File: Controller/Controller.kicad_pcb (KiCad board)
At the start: 2 copper layers, 213 x 25 mm, 94 parts, among them J1 CON_TLC, J2 CON_15V, J3 CON_ICSP, J4 DC out, J5 CON_5V, J6 CON_5V_AUX, J7 CON_USB_A, Q1 SI4435FDY, Q2 SI4435FDY, Q3 SQ2309ES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

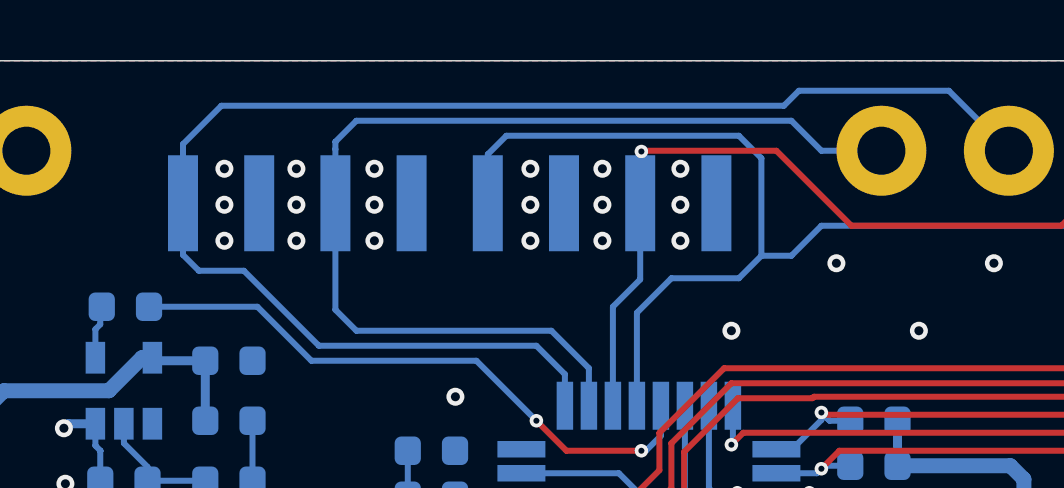
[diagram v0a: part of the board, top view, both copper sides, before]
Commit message: minor layout change.
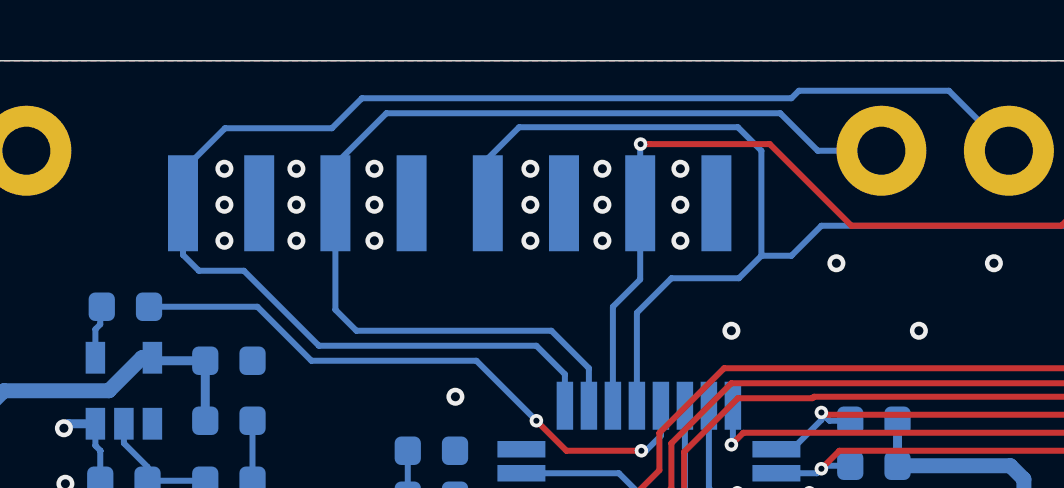
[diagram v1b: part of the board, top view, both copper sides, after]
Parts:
- removed the G*** at (239.0, 104.0)
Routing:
- net /TLC_BLANK: track 48.2 -> 47.7 mm

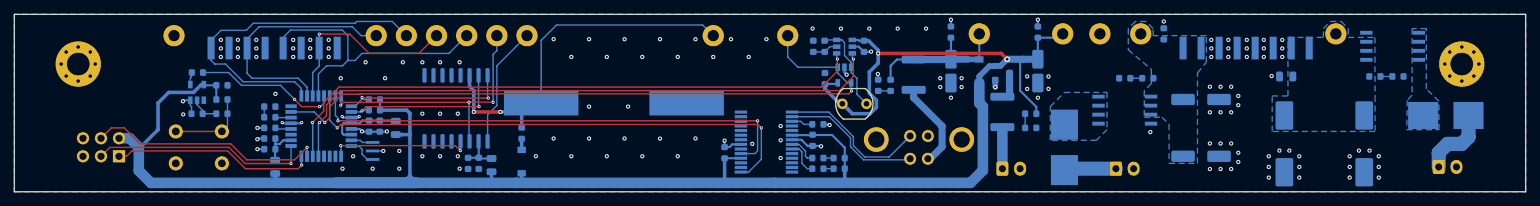
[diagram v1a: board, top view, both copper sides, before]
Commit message: Bug fixes: * Reset circuit   - netlabel RESET -> /RESET   - Reset button pulls high   - FTDI DTR connected to reset line * Added pull-ups to RTC outputs * Moved status LED to PC1 TODO: * Add thermal reliefs to copper planes
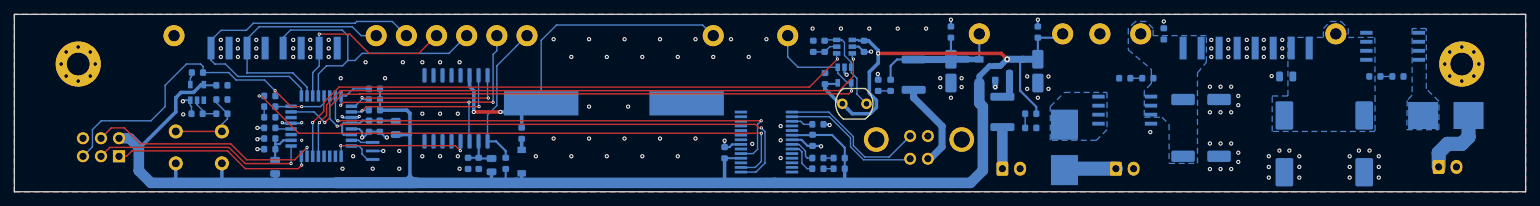
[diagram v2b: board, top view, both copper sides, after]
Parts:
- removed G***: LOGO, ak:lemonhead
- removed G***: LOGO, ak:LN-10x5mm
- added C27: 100nF, Capacitor_SMD:C_0603_1608Metric, B.Cu at (82.5, 104.5)
- added R16: 4k7, Resistor_SMD:R_0603_1608Metric, B.Cu at (97.2, 103.5)
- added R17: 4k7, Resistor_SMD:R_0603_1608Metric, B.Cu at (115.8, 114.0)
- F4: value MF-MSMF050-2 500mA -> 500mA
- R13: value 330R -> 1k
- moved SW1 7.91 mm to (75.8, 109.5), turned to 180 degrees
- moved D8 1.50 mm to (82.5, 107.5)
- moved R7 1.50 mm to (82.5, 106.0)
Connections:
- J3 pad 5: (no net) -> /~RESET~
- R11 pad 1: Net-(R11-Pad1) -> GND
- R11 pad 2: +5V -> Net-(R11-Pad2)
- R12 pad 2: Net-(R11-Pad1) -> Net-(R11-Pad2)
- SW1 pad 1: GND -> Net-(R11-Pad2)
- SW1 pad 2: Net-(R11-Pad1) -> +5V
- U1 pad 2: (no net) -> Net-(C27-Pad1)
- U2 pad 22: /LED -> (no net)
- U2 pad 24: (no net) -> /LED
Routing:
- net Net-(C27-Pad1): track 0.00 -> 80.9 mm, vias 0 -> 2
- net /~RESET~: track 20.4 -> 47.7 mm
- net Net-(R11-Pad2): track 0.00 -> 12.0 mm
- net Net-(R11-Pad1): track 11.3 -> 0.00 mm
- net +5V: track 283.5 -> 289.5 mm
- net /RTC_1PPS: track 38.3 -> 42.6 mm
- net /RTC_32K: track 17.2 -> 21.3 mm
- net GND: track 34.7 -> 36.2 mm
- net /~POT_CS~: track 85.0 -> 84.0 mm
- net /FTDI_TX: track 73.1 -> 73.9 mm
- net /FTDI_RX: track 69.6 -> 70.2 mm
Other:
- rule pad_to_mask_clearance: 0.051 -> 0.025

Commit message: Replaced LDR with PD, changed USB connector.
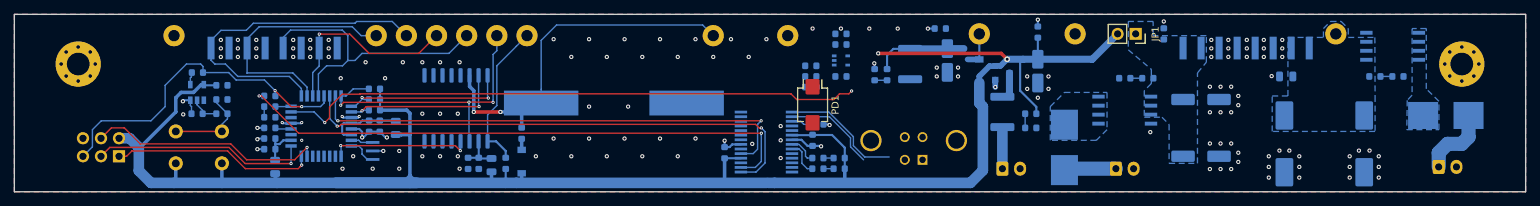
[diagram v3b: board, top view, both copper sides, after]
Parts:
- removed TP14, TP15: TestPoint_Alt, TestPoint:TestPoint_Loop_D2.60mm_Drill1.6mm_Beaded
- removed U6: MCP4012-xxxxCH, Package_TO_SOT_SMD:SOT-23-6
- added JP1: 5V PASSTHRU, Connector_PinSocket_2.54mm:PinSocket_1x02_P2.54mm_Vertical, F.Cu at (204.5, 95.8)
- added PD1: SFH 2440, OptoDevice:Osram_SMD-DIL2_4.5x4.0mm, F.Cu at (159.0, 105.8)
- added R18: ??, Resistor_SMD:R_0603_1608Metric, B.Cu at (158.8, 101.8)
- C23: value 10nF -> 1uF
- J7: footprint ak:UJ2-BV-1-TH -> Connector_USB:USB_B_TE_5787834_Vertical
- R10: value LDR07 -> ??; footprint OptoDevice:R_LDR_5.1x4.3mm_P3.4mm_Vertical -> Resistor_SMD:R_0603_1608Metric; moved to B.Cu
- R15: value 47k -> ??
- U5: value MCP6001-OT -> LMV301; footprint Package_TO_SOT_SMD:SOT-23-5 -> Package_TO_SOT_SMD:SOT-353_SC-70-5
- moved R10 6.96 mm to (158.8, 100.2), turned to 180 degrees
- moved C23 6.07 mm to (158.8, 103.2), turned to 180 degrees
- moved R15 3.91 mm to (163.0, 97.2), turned to 0 degrees
- moved C25 3.69 mm to (163.0, 95.8), turned to 180 degrees
- moved TP4 3.50 mm to (196.0, 95.8)
- moved C22 2.27 mm to (163.0, 101.8), turned to 180 degrees
- moved U5 2.11 mm to (163.0, 99.5), turned to 0 degrees
- moved J7 1.82 mm to (174.5, 113.5)
- moved C11 1.58 mm to (178.0, 99.5)
- moved C12 1.58 mm to (177.0, 95.0), turned to 180 degrees
- moved D5 1.58 mm to (167.8, 101.5)
- moved F4 1.58 mm to (172.8, 100.0)
- moved R4 1.58 mm to (169.5, 101.5)
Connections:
- C23 pad 1: Net-(C23-Pad1) -> GND
- C25 pad 1: +5V -> /PD_OUT
- C25 pad 2: GND -> Net-(C25-Pad2)
- R10 pad 1: +5V -> Net-(C23-Pad2)
- R10 pad 2: Net-(C23-Pad2) -> +5V
- R15 pad 1: GND -> Net-(C25-Pad2)
- R15 pad 2: Net-(C23-Pad1) -> /PD_OUT
- TP5 pad 1: /LDR -> /PD_OUT
- U1 pad 10: (no net) -> Net-(U1-Pad10)
- U1 pad 11: (no net) -> Net-(U1-Pad11)
- U1 pad 12: (no net) -> Net-(U1-Pad12)
- U1 pad 13: (no net) -> Net-(U1-Pad13)
- U1 pad 14: (no net) -> Net-(U1-Pad14)
- U1 pad 19: (no net) -> Net-(U1-Pad19)
- U1 pad 27: (no net) -> Net-(U1-Pad27)
- U1 pad 28: (no net) -> Net-(U1-Pad28)
- U1 pad 3: (no net) -> Net-(U1-Pad3)
- U1 pad 6: (no net) -> Net-(U1-Pad6)
- U1 pad 9: (no net) -> Net-(U1-Pad9)
- U2 pad 10: (no net) -> Net-(U2-Pad10)
- U2 pad 11: (no net) -> Net-(U2-Pad11)
- U2 pad 12: (no net) -> Net-(U2-Pad12)
- U2 pad 13: /POT_U~D~ -> Net-(U2-Pad13)
- U2 pad 14: /~POT_CS~ -> Net-(U2-Pad14)
- U2 pad 19: (no net) -> Net-(U2-Pad19)
- U2 pad 22: (no net) -> Net-(U2-Pad22)
- U2 pad 23: /LDR -> /PD_OUT
- U5 pad 1: /LDR -> Net-(C23-Pad2)
- U5 pad 3: Net-(C23-Pad2) -> Net-(C25-Pad2)
- U5 pad 4: /LDR -> /PD_OUT
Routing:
- net /LDR: track 97.5 -> 0.00 mm, vias 2 -> 0
- net /POT_U~D~: track 86.9 -> 0.00 mm, vias 2 -> 0
- net /~POT_CS~: track 84.0 -> 0.00 mm, vias 2 -> 0
- net /PD_OUT: track 0.00 -> 83.1 mm, vias 0 -> 2
- net +5V: track 289.5 -> 273.6 mm
- net Net-(C23-Pad2): track 13.2 -> 0.00 mm
- net Net-(F4-Pad2): track 12.4 -> 0.00 mm
- net /USBD-: track 20.0 -> 13.3 mm
- net /USBD+: track 21.2 -> 17.1 mm
- net GND: track 36.2 -> 32.1 mm, vias 153 -> 149
- net Net-(C23-Pad1): track 3.61 -> 0.00 mm
- net VBUS: track 22.0 -> 19.0 mm
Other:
- board text added: "PDOUT"
- board text removed: "LDR"

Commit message: Layout updated
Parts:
- J7: footprint Connector_USB:USB_B_TE_5787834_Vertical -> Connector_USB:USB_B_OST_USB-B1HSxx_Horizontal
- JP1: moved to B.Cu
- moved J7 10.8 mm to (172.0, 103.0), turned to 270 degrees
- moved C12 7.16 mm to (184.0, 96.5), turned to 270 degrees
- moved C22 5.80 mm to (163.8, 96.0), turned to 270 degrees
- moved D5 5.52 mm to (167.2, 96.0)
- moved R4 5.52 mm to (169.0, 96.0)
- moved C25 5.26 mm to (157.8, 96.0), turned to 270 degrees
- moved TP13 5.00 mm to (187.5, 95.8)
- moved D3 4.12 mm to (181.5, 97.0)
- moved R15 3.95 mm to (159.2, 96.0), turned to 90 degrees
- moved R10 3.82 mm to (162.5, 99.5), turned to 270 degrees
- moved U5 3.81 mm to (161.5, 96.0), turned to 90 degrees
- moved C23 3.76 mm to (159.0, 99.5), turned to 270 degrees
- moved R18 2.85 mm to (160.5, 99.5), turned to 90 degrees
- moved C11 2.55 mm to (177.5, 97.0)
- moved F4 2.55 mm to (172.2, 97.5)
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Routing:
- net GND: track 32.1 -> 54.8 mm, vias 149 -> 146
- net +5V: track 273.6 -> 286.3 mm
- net Net-(C25-Pad2): track 0.00 -> 12.5 mm, vias 0 -> 1
- net /USBD-: track 13.3 -> 24.4 mm
- net Net-(C23-Pad2): track 0.00 -> 6.65 mm
- net +BATT: track 50.0 -> 46.4 mm
- net Net-(F4-Pad2): track 0.00 -> 3.47 mm
- net /USBD+: track 17.1 -> 20.4 mm
- net /FTDI_RX: track 70.2 -> 69.3 mm
- net /~RESET~: track 47.7 -> 46.9 mm
- net /TLC_BLANK: track 47.7 -> 48.3 mm
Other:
- board text added: "5Vd|5V"
- board text added: "REV. B 03/2020"
- board text removed: "REV. A 10/2019"

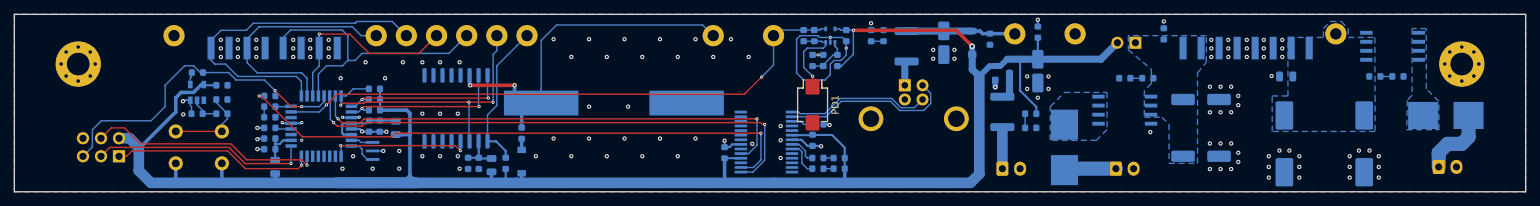
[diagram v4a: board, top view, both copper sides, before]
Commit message: shortened pcb by 1mm
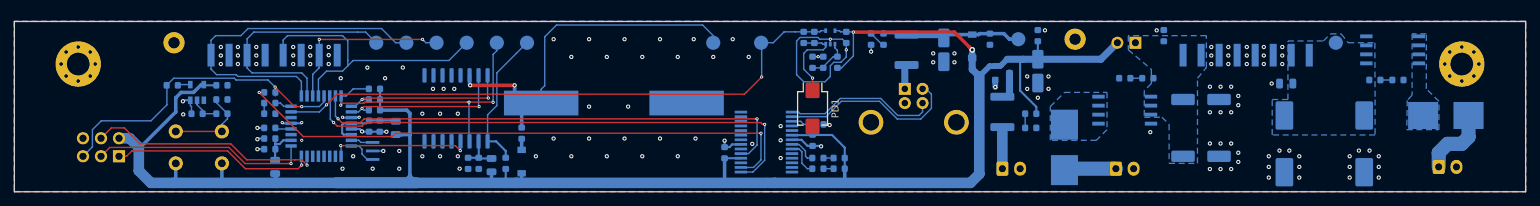
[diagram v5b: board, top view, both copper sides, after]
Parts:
- TP1, TP10, TP11, TP12, TP13, TP16, TP3, TP5, TP7, TP9: footprint TestPoint:TestPoint_Loop_D2.60mm_Drill1.6mm_Beaded -> TestPoint:TestPoint_Pad_D2.0mm
- moved R13 3.98 mm to (68.8, 103.0), turned to 0 degrees
- moved TP5 2.02 mm to (151.8, 97.0)
- moved TP16 1.25 mm to (232.8, 97.0)
- moved C11 1.00 mm to (177.5, 98.0)
- moved C3 1.00 mm to (225.8, 102.8)
- moved J1 1.00 mm to (92.0, 98.8)
- moved J4 1.00 mm to (229.0, 98.8)
- moved TP1 1.00 mm to (114.5, 97.0)
- moved TP10 1.00 mm to (97.5, 97.0)
- moved TP11 1.00 mm to (101.8, 97.0)
- moved TP12 1.00 mm to (145.0, 97.0)
- moved TP2 1.00 mm to (69.0, 97.0)
- moved TP3 1.00 mm to (118.8, 97.0)
- moved TP7 1.00 mm to (106.0, 97.0)
- moved TP9 1.00 mm to (110.2, 97.0)
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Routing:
- net /TLC_SDA: track 29.3 -> 26.5 mm, vias 1 -> 2
- net /USBD+: track 20.4 -> 22.4 mm
- net /USBD-: track 24.4 -> 26.0 mm
- net /TLC_SCL: track 41.1 -> 39.7 mm
- net VBUS: track 19.3 -> 20.6 mm
- net /~RESET~: track 46.9 -> 45.7 mm
- net /TLC_BLANK: track 48.3 -> 49.3 mm
- net /RTC_32K: track 21.3 -> 20.3 mm
- net /RTC_1PPS: track 42.6 -> 41.6 mm
- net +5V: track 286.3 -> 285.4 mm
- net Net-(D5-Pad2): track 1.75 -> 2.40 mm
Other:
- board size 213 x 25 mm -> 213 x 24 mm
- board text added: "5Vd->5V"
- board text removed: "5Vd|5V"

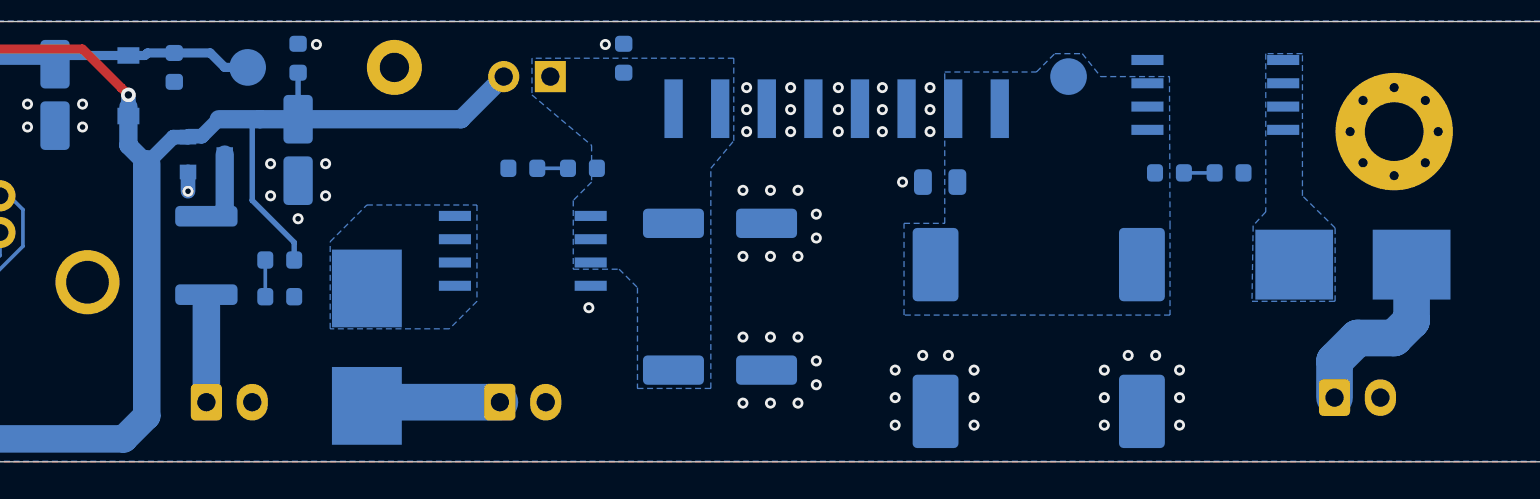
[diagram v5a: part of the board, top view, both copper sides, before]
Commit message: Replaced 15V connector. Created BOM and Gerbers
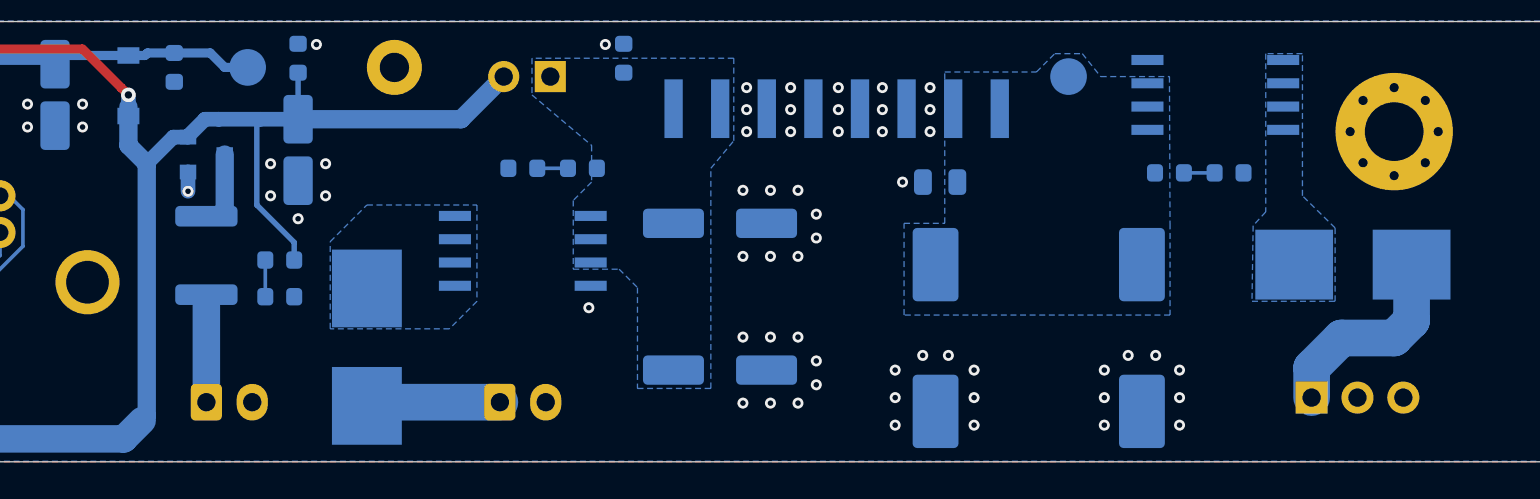
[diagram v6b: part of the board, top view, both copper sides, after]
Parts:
- C21, C22, C24: value 100n -> 100nF
- C25: value 100n -> ??
- D1: renamed from D9; value SS1P3L -> MBR130
- D2: renamed from D3; value SS1P3L -> MBR130
- F1: value 4A -> Fuse 4A
- F2: value 1A -> Fuse 1A
- F3, F4: value 500mA -> Polyfuse 500mA
- H1, H2: value MountingHole_Pad -> Mounting Hole
- J1: value CON_TLC -> DATA
- J2: value CON_15V -> 15V; footprint Connector_JST:JST_XH_B2B-XH-A_1x02_P2.50mm_Vertical -> Connectors_JST:JST_XH_B03B-XH-A_03x2.50mm_Straight
- J3: value CON_ICSP -> ICSP
- J4: value DC out -> DC OUT
- J5: value CON_5V -> 5V
- J6: value CON_5V_AUX -> 5V AUX
- J7: value CON_USB_A -> USB
- LD1: renamed from D1; value BLUE -> LED blue
- LD2: renamed from D2; value BLUE -> LED blue
- LD3: renamed from D4; value ORANGE -> LED orange
- LD4: renamed from D5; value GREEN -> LED green
- LD5: renamed from D6; value RX ORANGE -> LED orange
- LD6: renamed from D7; value TX GREEN -> LED green
- LD7: renamed from D8; value RED -> LED red
- SW1: value SW_Push -> RESET
- TP1: value TestPoint_Alt -> RTC_1PPS
- TP10: value TestPoint_Alt -> TLC_LAT
- TP11: value TestPoint_Alt -> TLC_BLANK
- TP12: value TestPoint_Alt -> +BATT
- TP13: value TestPoint_Alt -> VBUS
- TP16: value TestPoint_Alt -> +15V
- TP2, TP4: value TestPoint_Alt -> GND
- TP3: value TestPoint_Alt -> RTC_32K
- TP5: value TestPoint_Alt -> PD_OUT
- TP7: value TestPoint_Alt -> TLC_SDA
- TP9: value TestPoint_Alt -> TLC_SCL
- moved J2 1.25 mm to (246.0, 114.5)
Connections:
- U1 pad 10: Net-(U1-Pad10) -> (no net)
- U1 pad 11: Net-(U1-Pad11) -> (no net)
- U1 pad 12: Net-(U1-Pad12) -> (no net)
- U1 pad 13: Net-(U1-Pad13) -> (no net)
- U1 pad 14: Net-(U1-Pad14) -> (no net)
- U1 pad 19: Net-(U1-Pad19) -> (no net)
- U1 pad 27: Net-(U1-Pad27) -> (no net)
- U1 pad 28: Net-(U1-Pad28) -> (no net)
- U1 pad 3: Net-(U1-Pad3) -> (no net)
- U1 pad 6: Net-(U1-Pad6) -> (no net)
- U1 pad 9: Net-(U1-Pad9) -> (no net)
- U2 pad 10: Net-(U2-Pad10) -> (no net)
- U2 pad 11: Net-(U2-Pad11) -> (no net)
- U2 pad 12: Net-(U2-Pad12) -> (no net)
- U2 pad 13: Net-(U2-Pad13) -> (no net)
- U2 pad 14: Net-(U2-Pad14) -> (no net)
- U2 pad 19: Net-(U2-Pad19) -> (no net)
- U2 pad 22: Net-(U2-Pad22) -> (no net)
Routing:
- net +5V: track 285.4 -> 286.7 mm
- net Net-(F1-Pad2): track 10.2 -> 11.2 mm

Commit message: Assembly drawing
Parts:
- F3: value Polyfuse 500mA -> 0.5A
- F4: value Polyfuse 500mA -> 500mA
- LD1, LD2: value LED blue -> blue
- LD3, LD5: value LED orange -> orange
- LD4, LD6: value LED green -> green
- LD7: value LED red -> red
- U2: value ATmega328P-AU -> ATmega328P
